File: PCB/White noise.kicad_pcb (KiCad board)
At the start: 2 copper layers, 92.7 x 75 mm, 26 parts, among them J1 Conn_01x02_Pin, U1 ESP32-C3_SUPERMINI_TH, U2 AP2112K-3.3, U3 MCP73831-2-OT

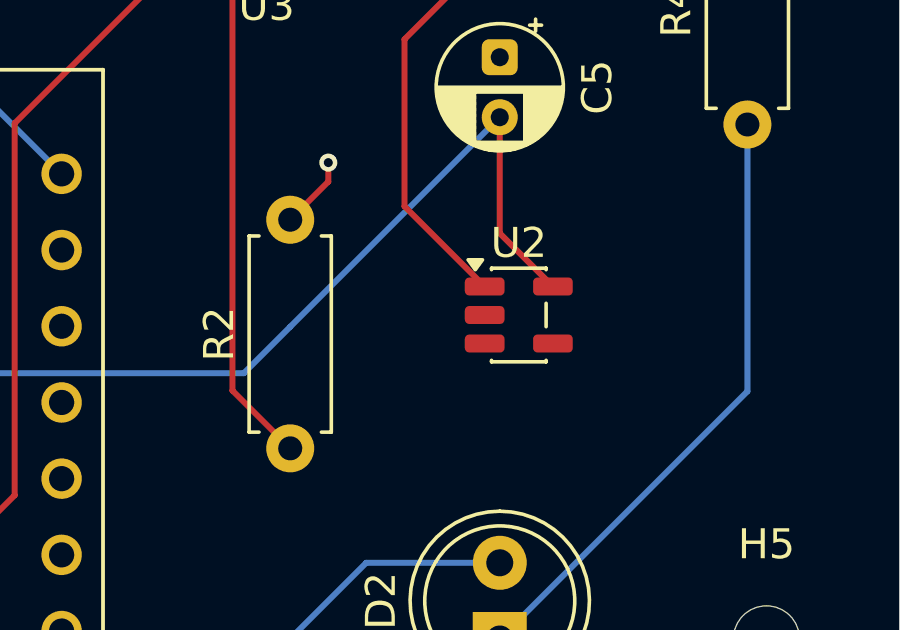
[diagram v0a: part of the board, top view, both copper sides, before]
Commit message: added source files and connected the en of volt regulator
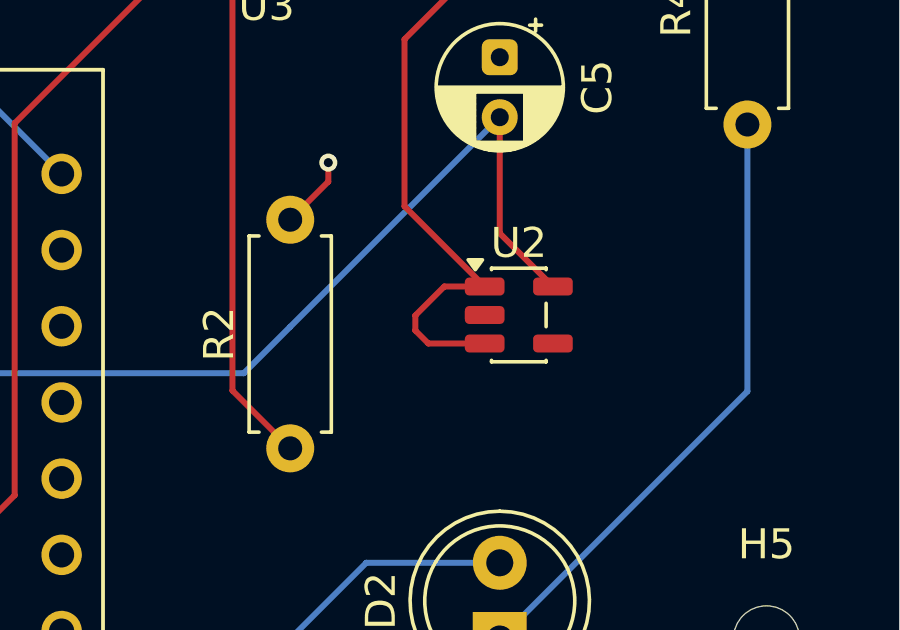
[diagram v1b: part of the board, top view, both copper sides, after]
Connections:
- BT1 pad P1: Net-(U2-VIN) -> Net-(U2-EN)
- BT1 pad P2: Net-(U2-VIN) -> Net-(U2-EN)
- C3 pad 2: Net-(U2-VIN) -> Net-(U2-EN)
- C4 pad 2: Net-(U2-VIN) -> Net-(U2-EN)
- U2 pad 1: Net-(U2-VIN) -> Net-(U2-EN)
- U2 pad 3: unconnected-(U2-EN-Pad3) -> Net-(U2-EN)
- U3 pad 3: Net-(U2-VIN) -> Net-(U2-EN)
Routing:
- net Net-(U2-EN): track 0.00 -> 164.0 mm, vias 0 -> 1
- net Net-(U2-VIN): track 158.3 -> 0.00 mm, vias 1 -> 0
